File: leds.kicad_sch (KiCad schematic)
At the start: 10 parts, among them U10 SK9822, U11 SK9822, U12 SK9822, U13 SK9822, U14 SK9822

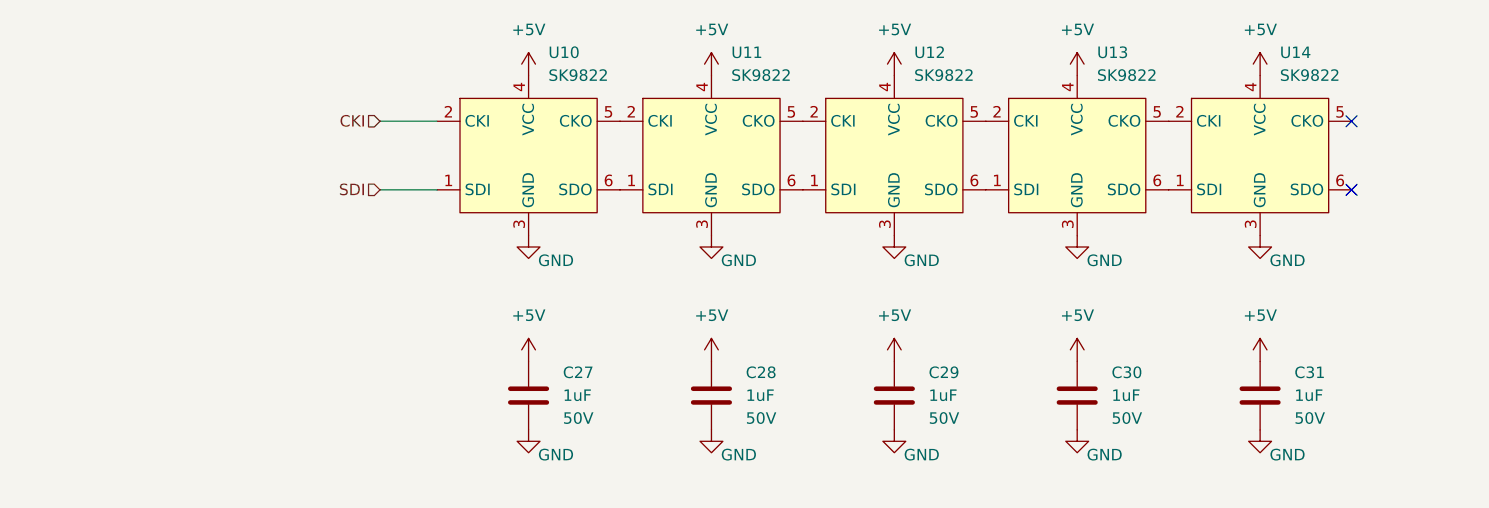
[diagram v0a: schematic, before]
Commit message: Replaced n-channel FETs, LDO, and SWD connector with Basic JLCPCB parts
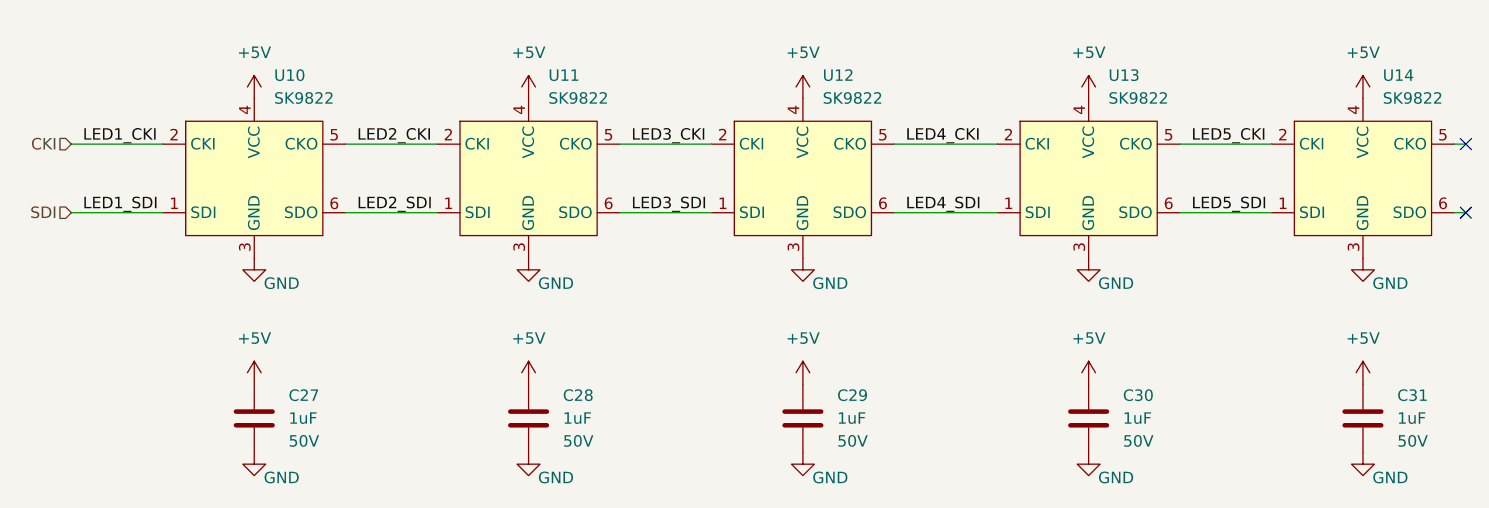
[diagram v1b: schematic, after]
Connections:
- net LED2_CKI: now reaches U10.5 (CKO), U11.2 (CKI)
- net LED2_SDI: now reaches U10.6 (SDO), U11.1 (SDI)
- net LED4_SDI: now reaches U12.6 (SDO), U13.1 (SDI)
- net LED4_CKI: now reaches U12.5 (CKO), U13.2 (CKI)
- net LED5_CKI: now reaches U13.5 (CKO), U14.2 (CKI)
- net LED5_SDI: now reaches U13.6 (SDO), U14.1 (SDI)
- net LED3_SDI: now reaches U11.6 (SDO), U12.1 (SDI)
- net LED3_CKI: now reaches U11.5 (CKO), U12.2 (CKI)
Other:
- moved on the sheet: C27, C28, C29, C30, C31, U10, U11, U12, U13, U14
